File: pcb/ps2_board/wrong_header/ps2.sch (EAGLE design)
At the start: 35 parts, among them IC3 STM32F042F4, SW4 324_SW, U1 MAX3232

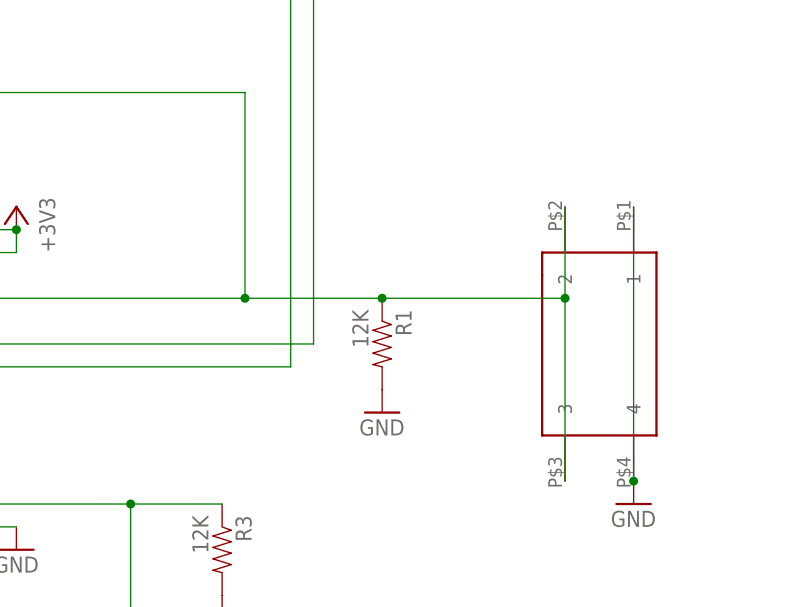
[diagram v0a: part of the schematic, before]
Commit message: serial mouse write working
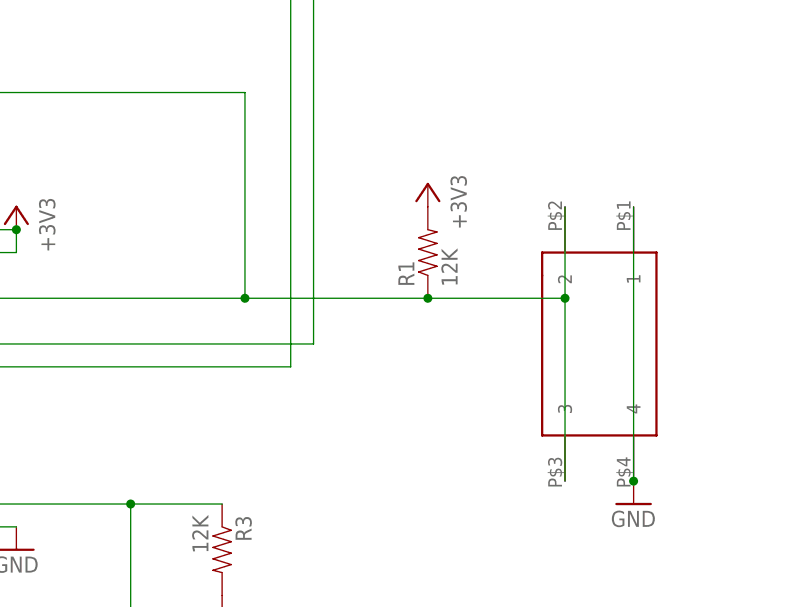
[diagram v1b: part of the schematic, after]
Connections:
- net +3V3: now also R1.2
- net GND: no longer R1.2
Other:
- moved on the sheet: R1
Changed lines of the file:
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@@
 <part name="GND8" library="supply1" deviceset="GND" device=""/>
 <part name="R1" library="SparkFun-Passives" deviceset="RESISTOR" device="0805-RES" value="12K"/>
-<part name="GND4" library="supply1" library_urn="urn:adsk.eagle:library:371" deviceset="GND" device=""/>
 <part name="JP4" library="pinhead" library_urn="urn:adsk.eagle:library:325" deviceset="PINHD-1X8" device="" package3d_urn="urn:adsk.eagle:package:22409/2"/>
 <part name="GND5" library="supply1" library_urn="urn:adsk.eagle:library:371" deviceset="GND" device=""/>
@@
 <part name="JP11" library="pinhead" library_urn="urn:adsk.eagle:library:325" deviceset="PINHD-1X4" device="" package3d_urn="urn:adsk.eagle:package:22407/2"/>
 <part name="+3V9" library="backplane" deviceset="+3V3" device=""/>
+<part name="+3V10" library="backplane" deviceset="+3V3" device=""/>
 </parts>
 <sheets>
@@
 <attribute name="VALUE" x="215.9" y="-35.56" size="1.778" layer="96" rot="MR0"/>
 </instance>
-<instance part="R1" gate="G$1" x="254" y="22.86" smashed="yes" rot="R270">
-<attribute name="NAME" x="255.4986" y="26.67" size="1.778" layer="95" rot="R270"/>
-<attribute name="VALUE" x="250.698" y="26.67" size="1.778" layer="96" rot="R270"/>
-</instance>
-<instance part="GND4" gate="1" x="254" y="15.24" smashed="yes">
-<attribute name="VALUE" x="251.46" y="12.7" size="1.778" layer="96"/>
+<instance part="R1" gate="G$1" x="259.08" y="33.02" smashed="yes" rot="R90">
+<attribute name="NAME" x="257.5814" y="29.21" size="1.778" layer="95" rot="R90"/>
+<attribute name="VALUE" x="262.382" y="29.21" size="1.778" layer="96" rot="R90"/>
 </instance>
 <instance part="JP4" gate="A" x="111.76" y="-43.18" smashed="yes" rot="MR270">
@@
 <instance part="+3V9" gate="G$1" x="248.92" y="134.62" smashed="yes" rot="MR0">
 <attribute name="VALUE" x="251.46" y="129.54" size="1.778" layer="96" rot="MR90"/>
+</instance>
+<instance part="+3V10" gate="G$1" x="259.08" y="40.64" smashed="yes" rot="MR0">
+<attribute name="VALUE" x="261.62" y="35.56" size="1.778" layer="96" rot="MR90"/>
 </instance>
 </instances>
@@
 <wire x1="251.46" y1="124.46" x2="254" y2="124.46" width="0.1524" layer="91"/>
 <junction x="251.46" y="124.46"/>
+</segment>
+<segment>
+<pinref part="R1" gate="G$1" pin="2"/>
+<pinref part="+3V10" gate="G$1" pin="+3V3"/>
 </segment>
 </net>
@@
 </segment>
 <segment>
-<pinref part="R1" gate="G$1" pin="2"/>
-<pinref part="GND4" gate="1" pin="GND"/>
-</segment>
-<segment>
 <pinref part="GND6" gate="1" pin="GND"/>
 <pinref part="JP5" gate="A" pin="1"/>
@@
 <pinref part="SW4" gate="G$1" pin="2"/>
 <wire x1="208.28" y1="27.94" x2="238.76" y2="27.94" width="0.1524" layer="91"/>
-<wire x1="238.76" y1="27.94" x2="254" y2="27.94" width="0.1524" layer="91"/>
-<wire x1="254" y1="27.94" x2="274.32" y2="27.94" width="0.1524" layer="91"/>
+<wire x1="238.76" y1="27.94" x2="259.08" y2="27.94" width="0.1524" layer="91"/>
+<wire x1="259.08" y1="27.94" x2="274.32" y2="27.94" width="0.1524" layer="91"/>
 <wire x1="274.32" y1="27.94" x2="274.32" y2="38.1" width="0.1524" layer="91"/>
 <pinref part="SW4" gate="G$1" pin="3"/>
@@
 <junction x="274.32" y="27.94"/>
 <pinref part="R1" gate="G$1" pin="1"/>
-<junction x="254" y="27.94"/>
+<junction x="259.08" y="27.94"/>
 <wire x1="238.76" y1="27.94" x2="238.76" y2="50.8" width="0.1524" layer="91"/>
 <wire x1="238.76" y1="50.8" x2="60.96" y2="50.8" width="0.1524" layer="91"/>
